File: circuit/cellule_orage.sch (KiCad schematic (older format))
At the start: 48 parts

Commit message: BOM update
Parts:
- gave numbers to parts that had none: 25
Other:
- note added: "DC-DC converter to generate 6 [V]"
- note added: "Linear regulator to generate 3 [V]"
- note added: "User feedback (LED and buzzer)"

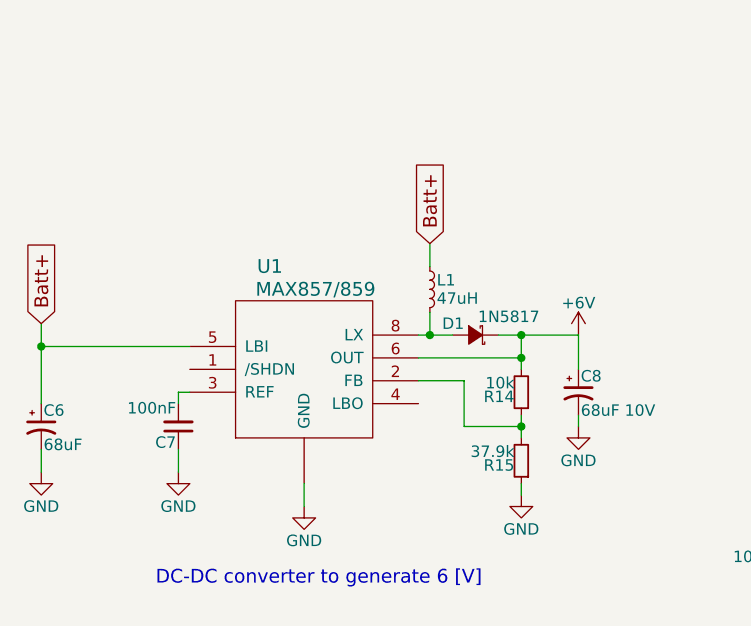
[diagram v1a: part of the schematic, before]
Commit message: Documentation update
Little value correction, add some component reference to BOM and correct
some type fault in report.
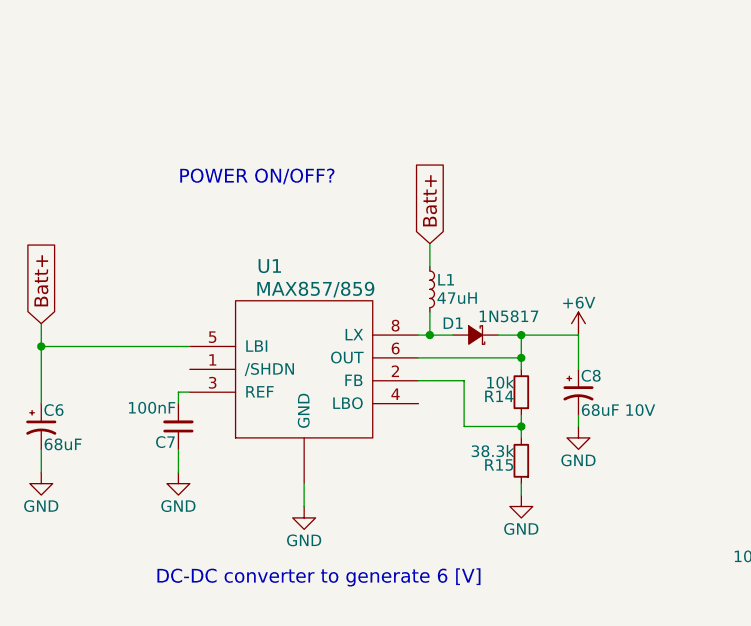
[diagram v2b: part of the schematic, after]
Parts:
- R15: value 37.9k -> 38.3k
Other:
- note added: "POWER ON/OFF?"
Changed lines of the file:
@@
 P 2850 5950
 F 0 "R15" H 2880 5970 50  0000 L CNN
-F 1 "37.9k" H 2880 5910 50  0000 L CNN
+F 1 "38.3k" H 2880 5910 50  0000 L CNN
 F 2 "" H 2850 5950 50  0000 C CNN
 F 3 "" H 2850 5950 50  0000 C CNN
@@
 Text Notes 8850 6450 0    60   ~ 0
 User feedback (LED and buzzer)
+Text Notes 1350 4750 0    60   ~ 0
+POWER ON/OFF?
 $EndSCHEMATC

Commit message: Schematic update
Added an ON/OFF switch, modified user reference and updated BOM
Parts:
- added R19: 38.3k, symbol R_Small
- added SW1: OFF/ON, symbol SPST
- R10: value 8.25k -> 4.99k
- R8: value 3.3k -> 4.99k
- R9: value 38.5k -> 50k
- SW2: renamed from SW1; value SWITCH_INV -> USER/AUTO
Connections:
- wire segments 122 -> 128

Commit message: Documentation update
Some change on schematic after discussion with all the group, nothing
confirmed yet
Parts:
- removed C1: 4.7uF, symbol CP1_Small
- removed P1: Phototransistor BPW85, symbol CONN_01X02
- removed R1: 100, symbol R_Small
- removed R2: 5.9k, symbol R_Small
- removed SW2: USER/AUTO, symbol SWITCH_INV
- added P? (x2): Batt+, symbol CONN_01X01
- added P? (x2): Batt-, symbol CONN_01X01
- added P?: Buzzer ON/OFF, symbol CONN_01X03
- added P?: LED ON/OFF, symbol CONN_01X03
- added P? (x3): Phototransistor BPW85, symbol CONN_01X02
- added P?: AUTO/USER, symbol CONN_01X03
- added P?: OUTPUT, symbol CONN_01X07
- added R? (x3): 100, symbol R_Small
- added R? (x3): 5.9k, symbol R_Small
- R4, R9: symbol POT -> POT-RESCUE-cellule_orage
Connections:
- net labels added: BUZZER_OUT, LED_OUT, LEVEL, TRIG_OUT
- wire segments 128 -> 167
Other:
- note added: "Additioneur"
- note added: "Battery holder"
- note added: "Capteurs"
- note added: "POWER ON/OFF"
- note removed: "Capteur"
- note removed: "POWER ON/OFF?"
- moved on the sheet: C10, C11, C12, C2, C3, C4, C5, C6, C7, C8, C9, D1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

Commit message: Little doc update
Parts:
- removed R? (x2): 100, symbol R_Small
- removed R? (x2): 5.9k, symbol R_Small
- added P?: USB_OTG, symbol USB_OTG
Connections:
- net at C2.2: now also P?.2 (P2), P?.2 (P2), P?.2 (P2), R?.1
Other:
- note removed: "Additioneur"
- moved on the sheet: C10, C11, C12, C2, C3, C4, C5, C6, C7, C8, C9, D1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

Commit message: Small updates
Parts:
- removed J1: Jack_3.5mm_3pin, symbol Jack_3.5mm_3pin
- removed U1: MAX857/859, symbol MAX857/859
- removed U3: NCP4586, symbol NCP4586
- added J?: Jack_3.5mm_3pin, symbol Jack_3.5mm_3pin
- added U?: MAX857/859, symbol MAX857/859
- added U?: NCP4586, symbol NCP4586
- added U?: MAX14578AE, symbol MAX14578AE
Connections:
- net +3V: now also U?.5 (Vout)
- net +6V: now also U?.1 (Vin), U?.3 (/CE), U?.6 (OUT)
- net Batt+: now also U?.5 (LBI)
- net GND: now also U?.1 (/SHDN), U?.2 (GND), U?.~ (GND)
- net at R14.1, R15.2: now also U?.2 (FB)
- net at C7.2: now also U?.3 (REF)
- net at D1.2 (A), L1.2: now also U?.8 (LX)
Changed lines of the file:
@@
 EESchema Schematic File Version 2
-LIBS:cellule_orage-rescue
 LIBS:power
 LIBS:device
@@
 LIBS:contrib
 LIBS:valves
+LIBS:maxim_integrated
+LIBS:on_semiconductor
+LIBS:audio_divers
 LIBS:cellule_orage-cache
 EELAYER 25 0
@@
 	1    0    0    -1
 $EndComp
-$Comp
-L Jack_3.5mm_3pin J1
-U 1 1 577A8E90
-P 12650 1400
-F 0 "J1" H 12650 1650 60  0000 C CNN
-F 1 "Jack_3.5mm_3pin" H 12650 1150 60  0000 C CNN
-F 2 "" H 12650 1400 60  0000 C CNN
-F 3 "" H 12650 1400 60  0000 C CNN
-	1    12650 1400
-	1    0    0    -1
-$EndComp
 Wire Wire Line
 	11350 2850 11350 2950
@@
 $EndComp
 $Comp
-L MAX857/859 U1
-U 1 1 57875DC3
-P 2900 9350
-F 0 "U1" H 2750 9800 60  0000 C CNN
-F 1 "MAX857/859" H 2950 9700 60  0000 C CNN
-F 2 "" H 2900 9350 60  0000 C CNN
-F 3 "" H 2900 9350 60  0000 C CNN
-	1    2900 9350
-	1    0    0    -1
-$EndComp
-$Comp
 L L_Small L1
 U 1 1 57875EAE
@@
 Wire Wire Line
 	2350 9450 2400 9450
-$Comp
-L NCP4586 U3
-U 1 1 5788655F
-P 5650 10250
-F 0 "U3" H 5650 10750 60  0000 C CNN
-F 1 "NCP4586" H 5650 10650 60  0000 C CNN
-F 2 "" H 5650 10250 60  0000 C CNN
-F 3 "" H 5650 10250 60  0000 C CNN
-	1    5650 10250
-	1    0    0    -1
-$EndComp
 $Comp
 L C_Small C10
@@
 	0    -1   -1   0
 $EndComp
+$Comp
+L MAX857/859 U?
+U 1 1 57F6590E
+P 2900 9350
+F 0 "U?" H 2750 9800 60  0000 C CNN
+F 1 "MAX857/859" H 2950 9700 60  0000 C CNN
+F 2 "" H 2900 9350 60  0000 C CNN
+F 3 "" H 2900 9350 60  0000 C CNN
+	1    2900 9350
+	1    0    0    -1
+$EndComp
+$Comp
+L NCP4586 U?
+U 1 1 57F67677
+P 5650 10250
+F 0 "U?" H 5650 10750 60  0000 C CNN
+F 1 "NCP4586" H 5650 10650 60  0000 C CNN
+F 2 "" H 5650 10250 60  0000 C CNN
+F 3 "" H 5650 10250 60  0000 C CNN
+	1    5650 10250
+	1    0    0    -1
+$EndComp
+$Comp
+L Jack_3.5mm_3pin J?
+U 1 1 57F68248
+P 12700 1400
+F 0 "J?" H 12700 1650 60  0000 C CNN
+F 1 "Jack_3.5mm_3pin" H 12700 1150 60  0000 C CNN
+F 2 "" H 12700 1400 60  0000 C CNN
+F 3 "" H 12700 1400 60  0000 C CNN
+	1    12700 1400
+	1    0    0    -1
+$EndComp
+$Comp
+L MAX14578AE U?
+U 1 1 57F6C9D2
+P 3950 5850
+F 0 "U?" H 4250 5150 60  0000 C CNN
+F 1 "MAX14578AE" H 4450 5050 60  0000 C CNN
+F 2 "" H 3950 5850 60  0001 C CNN
+F 3 "" H 3950 5850 60  0001 C CNN
+	1    3950 5850
+	1    0    0    -1
+$EndComp
 $EndSCHEMATC

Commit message: Charger update
Add a battery charger and update documentation in consequence.
Fix some typo and schematic details
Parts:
- removed U?: MAX14578AE, symbol MAX14578AE
- added C? (x2): 4.7uF, symbol CP1_Small
- added D?: CHRG_STATUS_RED 2[mA], symbol Led_Small
- added R?: 2k, symbol R_Small
- added R?: 1.65k, symbol R_Small
- added U?: MCP73831/2, symbol MCP73831/2
- D2: value Red 2[mA] -> TRIG_RED 2[mA]
- J?: value Jack_3.5mm_3pin -> Jack_2.5mm_3pin
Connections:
- net Batt+: now also C?.1, U?.3 (Vbat)
- net GND: now also P?.5 (GND), P?.6 (shield), C?.2, C?.2, R?.2, U?.2 (Vss)
- net TRIG_OUT: now also J?.2 (T), U5.4
- net at U5.3: now also J?.1 (S)
- net at P?.1 (VCC): now also C?.1, D?.2 (A), U?.4 (Vdd)
- new net: R?.1, U?.1 (STAT)
- new net: R?.1, U?.5 (PROG)
- new net: D?.1 (K), R?.2
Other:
- note added: "Micro USB-B battery charger"
- note added: "Modifier LBI LBO"
- note added: "Shutter - Focus - GND\nTip - Ring - Sleeve\nValid for Nikon/Canon"
- note removed: "Ordre à définir"
- moved on the sheet: J?, P?
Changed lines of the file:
@@
 LIBS:on_semiconductor
 LIBS:audio_divers
+LIBS:microchip_divers
 LIBS:cellule_orage-cache
 EELAYER 25 0
@@
 Wire Wire Line
 	10900 1800 11050 1800
-Text Notes 13000 1400 0    60   ~ 0
-Ordre à définir
-$Comp
-L GND #PWR35
-U 1 1 5774F895
-P 12350 1750
-F 0 "#PWR35" H 12350 1500 50  0001 C CNN
-F 1 "GND" H 12350 1600 50  0000 C CNN
-F 2 "" H 12350 1750 50  0000 C CNN
-F 3 "" H 12350 1750 50  0000 C CNN
-	1    12350 1750
-	1    0    0    -1
-$EndComp
-Wire Wire Line
-	12050 1250 12350 1250
-Wire Wire Line
-	12050 1450 12200 1450
-Wire Wire Line
-	12200 1450 12200 1350
-Wire Wire Line
-	12200 1350 12350 1350
+Text Notes 13150 1350 0    60   ~ 0
+Shutter - Focus - GND\nTip - Ring - Sleeve\nValid for Nikon/Canon
+Wire Wire Line
+	12050 1250 12700 1250
+Wire Wire Line
+	12050 1450 12700 1450
 Text GLabel 10850 3750 0    60   Input ~ 0
 Timer_out
@@
 P 11350 3350
 F 0 "D2" H 11300 3475 50  0000 L CNN
-F 1 "Red 2[mA]" H 11175 3250 50  0000 L CNN
+F 1 "TRIG_RED 2[mA]" H 11150 3100 50  0000 L CNN
 F 2 "" V 11350 3350 50  0000 C CNN
 F 3 "" V 11350 3350 50  0000 C CNN
@@
 	1750 3500 1400 3500
 $Comp
-L USB_OTG P?
-U 1 1 57F1F609
-P 1600 5750
-F 0 "P?" H 1925 5625 50  0000 C CNN
-F 1 "USB_OTG" H 1600 5950 50  0000 C CNN
-F 2 "" V 1550 5650 50  0000 C CNN
-F 3 "" V 1550 5650 50  0000 C CNN
-	1    1600 5750
-	0    -1   -1   0
-$EndComp
-$Comp
 L MAX857/859 U?
 U 1 1 57F6590E
@@
 L Jack_3.5mm_3pin J?
 U 1 1 57F68248
-P 12700 1400
-F 0 "J?" H 12700 1650 60  0000 C CNN
-F 1 "Jack_3.5mm_3pin" H 12700 1150 60  0000 C CNN
-F 2 "" H 12700 1400 60  0000 C CNN
-F 3 "" H 12700 1400 60  0000 C CNN
-	1    12700 1400
-	1    0    0    -1
-$EndComp
-$Comp
-L MAX14578AE U?
-U 1 1 57F6C9D2
-P 3950 5850
-F 0 "U?" H 4250 5150 60  0000 C CNN
-F 1 "MAX14578AE" H 4450 5050 60  0000 C CNN
-F 2 "" H 3950 5850 60  0001 C CNN
-F 3 "" H 3950 5850 60  0001 C CNN
-	1    3950 5850
-	1    0    0    -1
-$EndComp
+P 12850 1200
+F 0 "J?" H 12850 1450 60  0000 C CNN
+F 1 "Jack_2.5mm_3pin" H 12850 950 60  0000 C CNN
+F 2 "" H 12850 1200 60  0000 C CNN
+F 3 "" H 12850 1200 60  0000 C CNN
+	1    12850 1200
+	1    0    0    1
+$EndComp
+$Comp
+L MCP73831/2 U?
+U 1 1 57FC9F5C
+P 2700 7650
+F 0 "U?" H 2500 7850 60  0000 C CNN
+F 1 "MCP73831/2" H 2700 7400 60  0000 C CNN
+F 2 "" H 2700 7650 60  0001 C CNN
+F 3 "" H 2700 7650 60  0001 C CNN
+	1    2700 7650
+	1    0    0    -1
+$EndComp
+$Comp
+L USB_OTG P?
+U 1 1 57F1F609
+P 800 7750
+F 0 "P?" H 1125 7625 50  0000 C CNN
+F 1 "USB_OTG" H 800 7950 50  0000 C CNN
+F 2 "" V 750 7650 50  0000 C CNN
+F 3 "" V 750 7650 50  0000 C CNN
+	1    800  7750
+	0    -1   1    0
+$EndComp
+Text GLabel 4000 7550 2    60   Input ~ 0
+Batt+
+$Comp
+L R_Small R?
+U 1 1 57FCBC70
+P 3400 7800
+F 0 "R?" H 3430 7820 50  0000 L CNN
+F 1 "2k" H 3430 7760 50  0000 L CNN
+F 2 "" H 3400 7800 50  0000 C CNN
+F 3 "" H 3400 7800 50  0000 C CNN
+	1    3400 7800
+	1    0    0    -1
+$EndComp
+$Comp
+L GND #PWR?
+U 1 1 57FCC70A
+P 3400 8000
+F 0 "#PWR?" H 3400 7750 50  0001 C CNN
+F 1 "GND" H 3400 7850 50  0000 C CNN
+F 2 "" H 3400 8000 50  0000 C CNN
+F 3 "" H 3400 8000 50  0000 C CNN
+	1    3400 8000
+	1    0    0    -1
+$EndComp
+$Comp
+L GND #PWR?
+U 1 1 57FCC809
+P 3150 8000
+F 0 "#PWR?" H 3150 7750 50  0001 C CNN
+F 1 "GND" H 3150 7850 50  0000 C CNN
+F 2 "" H 3150 8000 50  0000 C CNN
+F 3 "" H 3150 8000 50  0000 C CNN
+	1    3150 8000
+	1    0    0    -1
+$EndComp
+$Comp
+L GND #PWR?
+U 1 1 57FCC8CB
+P 700 8200
+F 0 "#PWR?" H 700 7950 50  0001 C CNN
+F 1 "GND" H 700 8050 50  0000 C CNN
+F 2 "" H 700 8200 50  0000 C CNN
+F 3 "" H 700 8200 50  0000 C CNN
+	1    700  8200
+	1    0    0    -1
+$EndComp
+$Comp
+L GND #PWR?
+U 1 1 57FCC98D
+P 1100 8050
+F 0 "#PWR?" H 1100 7800 50  0001 C CNN
+F 1 "GND" H 1100 7900 50  0000 C CNN
+F 2 "" H 1100 8050 50  0000 C CNN
+F 3 "" H 1100 8050 50  0000 C CNN
+	1    1100 8050
+	1    0    0    -1
+$EndComp
+Wire Wire Line
+	1100 7550 2250 7550
+Wire Wire Line
+	3150 7550 4000 7550
+Wire Wire Line
+	3150 7650 3400 7650
+Wire Wire Line
+	3400 7650 3400 7700
+Wire Wire Line
+	3400 7900 3400 8000
+Wire Wire Line
+	3150 7750 3150 8000
+Wire Wire Line
+	1100 7950 1100 8050
+Wire Wire Line
+	700  8150 700  8200
+$Comp
+L CP1_Small C?
+U 1 1 57FCD3A5
+P 3700 7700
+F 0 "C?" H 3710 7770 50  0000 L CNN
+F 1 "4.7uF" H 3710 7620 50  0000 L CNN
+F 2 "" H 3700 7700 50  0000 C CNN
+F 3 "" H 3700 7700 50  0000 C CNN
+	1    3700 7700
+	1    0    0    -1
+$EndComp
+$Comp
+L CP1_Small C?
+U 1 1 57FCD47F
+P 1300 7700
+F 0 "C?" H 1310 7770 50  0000 L CNN
+F 1 "4.7uF" H 1310 7620 50  0000 L CNN
+F 2 "" H 1300 7700 50  0000 C CNN
+F 3 "" H 1300 7700 50  0000 C CNN
+	1    1300 7700
+	1    0    0    -1
+$EndComp
+$Comp
+L GND #PWR?
+U 1 1 57FCE07F
+P 1300 7850
+F 0 "#PWR?" H 1300 7600 50  0001 C CNN
+F 1 "GND" H 1300 7700 50  0000 C CNN
+F 2 "" H 1300 7850 50  0000 C CNN
+F 3 "" H 1300 7850 50  0000 C CNN
+	1    1300 7850
+	1    0    0    -1
+$EndComp
+$Comp
+L GND #PWR?
+U 1 1 57FCE147
+P 3700 7900
+F 0 "#PWR?" H 3700 7650 50  0001 C CNN
+F 1 "GND" H 3700 7750 50  0000 C CNN
+F 2 "" H 3700 7900 50  0000 C CNN
+F 3 "" H 3700 7900 50  0000 C CNN
+	1    3700 7900
+	1    0    0    -1
+$EndComp
+Wire Wire Line
+	1300 7600 1300 7550
+Connection ~ 1300 7550
+Wire Wire Line
+	1300 7850 1300 7800
+Wire Wire Line
+	3700 7900 3700 7800
+Wire Wire Line
+	3700 7600 3700 7550
+Connection ~ 3700 7550
+$Comp
+L R_Small R?
+U 1 1 57FCFD5E
+P 2050 7750
+F 0 "R?" H 2080 7770 50  0000 L CNN
+F 1 "1.65k" H 2080 7710 50  0000 L CNN
+F 2 "" H 2050 7750 50  0000 C CNN
+F 3 "" H 2050 7750 50  0000 C CNN
+	1    2050 7750
+	0    1    -1   0
+$EndComp
+$Comp
+L Led_Small D?
+U 1 1 57FD3850
+P 1750 7750
+F 0 "D?" H 1750 7650 50  0000 L CNN
+F 1 "CHRG_STATUS_RED 2[mA]" H 1150 7900 50  0000 L CNN
+F 2 "" V 1750 7750 50  0000 C CNN
+F 3 "" V 1750 7750 50  0000 C CNN
+	1    1750 7750
+	-1   0    0    1
+$EndComp
+Wire Wire Line
+	2250 7750 2150 7750
+Wire Wire Line
+	1950 7750 1850 7750
+Wire Wire Line
+	1650 7750 1550 7750
+Wire Wire Line
+	1550 7750 1550 7550
+Connection ~ 1550 7550
+Text Notes 2150 7300 0    60   ~ 0
+Micro USB-B battery charger
+Text Notes 4650 9000 0    60   ~ 0
+Modifier LBI LBO
+Wire Wire Line
+	12700 1450 12700 1350
+Wire Wire Line
+	12350 1050 12350 1250
+Connection ~ 12350 1250
 $EndSCHEMATC
